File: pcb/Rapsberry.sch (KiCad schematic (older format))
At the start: 1 part, among them P1 CONN_RASPBERRY

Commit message: getting  roo for sensors
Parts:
- P1: footprint TH:RPI_MATRIX_40 -> SMD:SMD_CONN_2x20
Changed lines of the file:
@@
 $Descr A4 11693 8268
 encoding utf-8
-Sheet 7 8
+Sheet 6 8
 Title ""
 Date ""
@@
 F 0 "P1" H 3825 3565 50  0000 C CNN
 F 1 "CONN_RASPBERRY" H 3825 3474 50  0000 C CNN
-F 2 "TH:RPI_MATRIX_40" H 3825 3481 60  0001 C CNN
+F 2 "SMD:SMD_CONN_2x20" H 3825 3481 60  0001 C CNN
 F 3 "" H 3300 1450 60  0000 C CNN
 	1    4100 2400

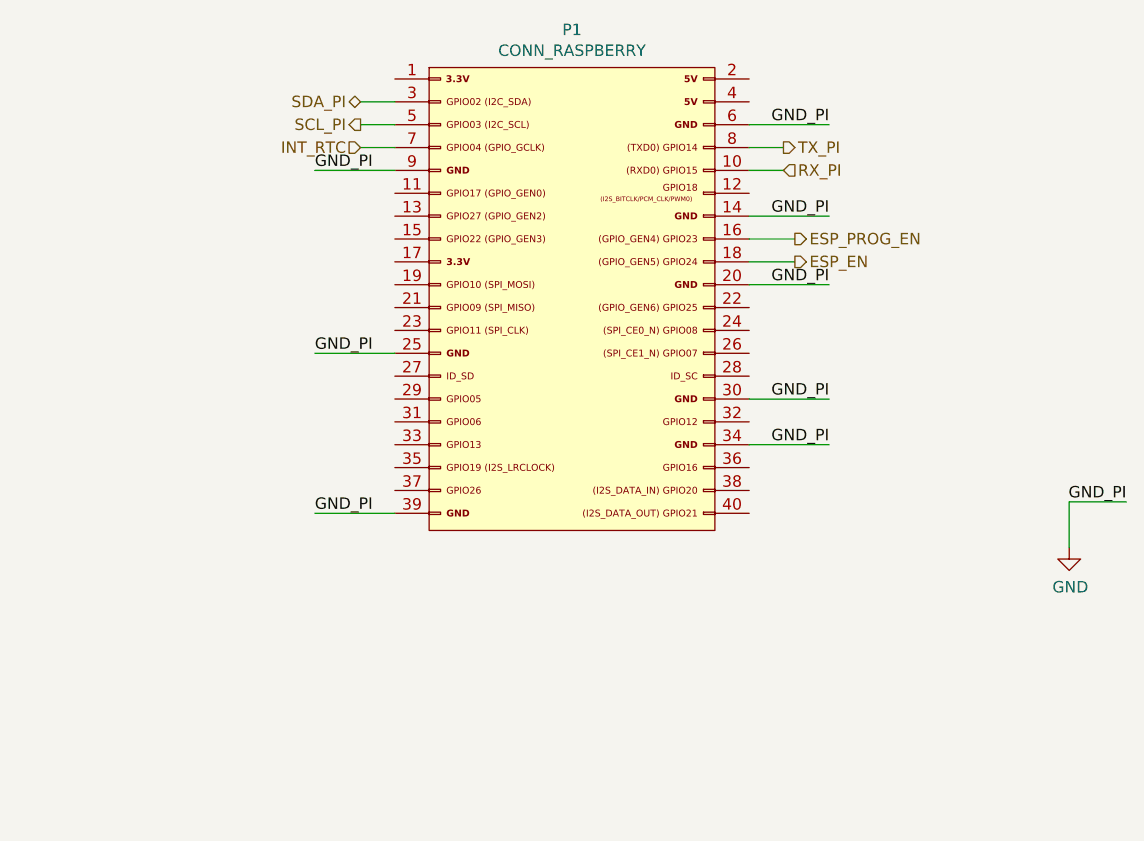
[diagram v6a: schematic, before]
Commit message: SPI connections between FPGA, PI and FLASH
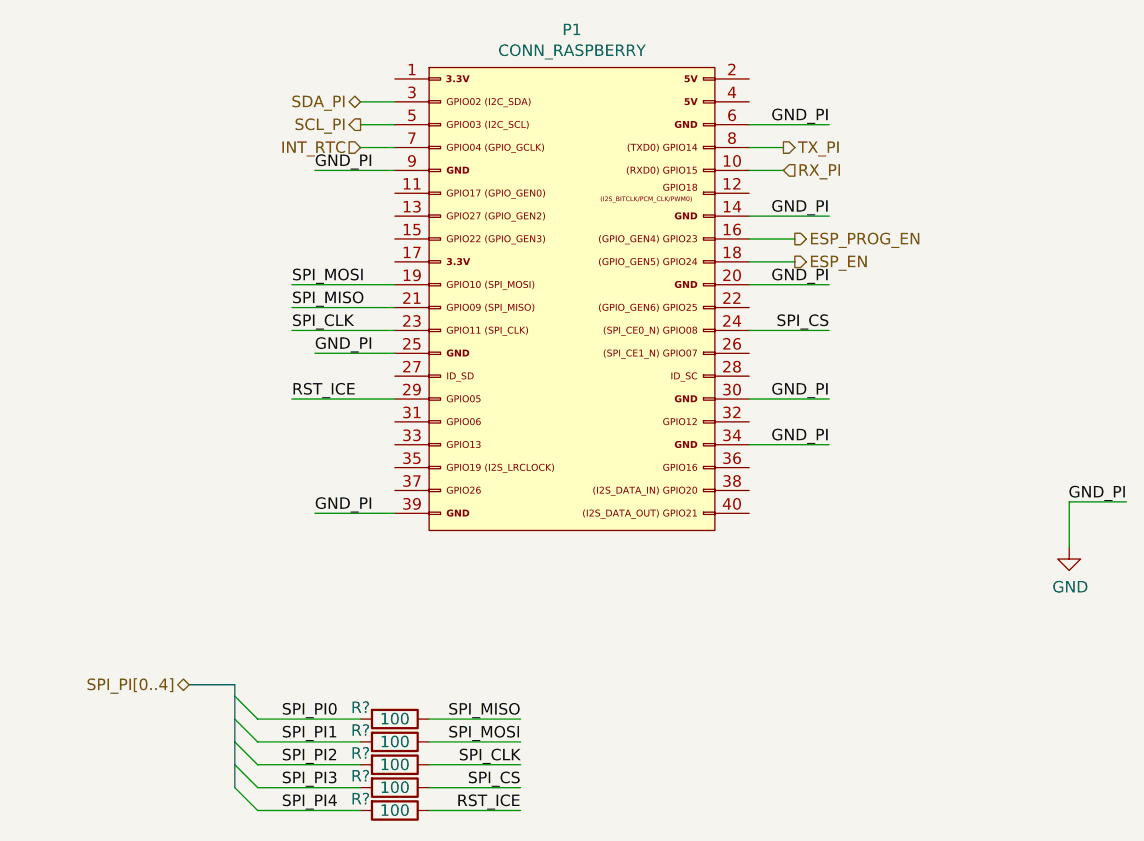
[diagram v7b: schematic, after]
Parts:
- added R? (x5): 100, symbol Device:R
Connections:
- net SPI_MOSI: now reaches P1.19 (P19)
- net SPI_MOSI: now also R?.1
- net SPI_MISO: now reaches P1.21 (P21)
- net SPI_MISO: now also R?.1
- net SPI_CLK: now reaches P1.23 (P23)
- net SPI_CLK: now also R?.1
- net SPI_CS: now reaches P1.24 (P24)
- net SPI_CS: now also R?.1
- net RST_ICE: now reaches P1.29 (P29)
- net RST_ICE: now also R?.1
- new net SPI_PI0: R?.2
- new net SPI_PI1: R?.2
- new net SPI_PI2: R?.2
- new net SPI_PI3: R?.2
- new net SPI_PI4: R?.2
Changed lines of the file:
@@
 Text Label 6250 3300 2    50   ~ 0
 GND_PI
+Text HLabel 2150 4100 0    50   BiDi ~ 0
+SPI_PI[0..4]
+Wire Bus Line
+	2150 4100 2350 4100
+Entry Wire Line
+	2350 4150 2450 4250
+Entry Wire Line
+	2350 4250 2450 4350
+Entry Wire Line
+	2350 4350 2450 4450
+Entry Wire Line
+	2350 4450 2450 4550
+Entry Wire Line
+	2350 4550 2450 4650
+Text Label 2800 4250 2    50   ~ 0
+SPI_PI0
+Text Label 2800 4350 2    50   ~ 0
+SPI_PI1
+Text Label 2800 4450 2    50   ~ 0
+SPI_PI2
+Text Label 2800 4550 2    50   ~ 0
+SPI_PI3
+Text Label 2800 4650 2    50   ~ 0
+SPI_PI4
+Text Label 2600 2350 0    50   ~ 0
+SPI_MOSI
+Text Label 2600 2450 0    50   ~ 0
+SPI_MISO
+Text Label 2600 2550 0    50   ~ 0
+SPI_CLK
+Text Label 4950 2550 2    50   ~ 0
+SPI_CS
+Wire Wire Line
+	2600 2350 3050 2350
+Wire Wire Line
+	2600 2450 3050 2450
+Wire Wire Line
+	2600 2550 3050 2550
+Wire Wire Line
+	4950 2550 4600 2550
+Text Label 3600 4250 2    50   ~ 0
+SPI_MISO
+Text Label 3600 4350 2    50   ~ 0
+SPI_MOSI
+Text Label 3600 4450 2    50   ~ 0
+SPI_CLK
+Text Label 3600 4550 2    50   ~ 0
+SPI_CS
+Text Label 2600 2850 0    50   ~ 0
+RST_ICE
+Wire Wire Line
+	2600 2850 3050 2850
+Text Label 3600 4650 2    50   ~ 0
+RST_ICE
+Wire Wire Line
+	2450 4250 2900 4250
+Wire Wire Line
+	2450 4350 2900 4350
+Wire Wire Line
+	2450 4450 2900 4450
+Wire Wire Line
+	2450 4550 2900 4550
+Wire Wire Line
+	2450 4650 2900 4650
+$Comp
+L Device:R R?
+U 1 1 5E9EA326
+P 3050 4250
+F 0 "R?" V 3000 4100 50  0000 C CNN
+F 1 "100" V 3050 4250 50  0000 C CNN
+F 2 "" V 2980 4250 50  0001 C CNN
+F 3 "~" H 3050 4250 50  0001 C CNN
+	1    3050 4250
+	0    1    1    0
+$EndComp
+$Comp
+L Device:R R?
+U 1 1 5EA15CD3
+P 3050 4350
+F 0 "R?" V 3000 4200 50  0000 C CNN
+F 1 "100" V 3050 4350 50  0000 C CNN
+F 2 "" V 2980 4350 50  0001 C CNN
+F 3 "~" H 3050 4350 50  0001 C CNN
+	1    3050 4350
+	0    1    1    0
+$EndComp
+$Comp
+L Device:R R?
+U 1 1 5EA17179
+P 3050 4450
+F 0 "R?" V 3000 4300 50  0000 C CNN
+F 1 "100" V 3050 4450 50  0000 C CNN
+F 2 "" V 2980 4450 50  0001 C CNN
+F 3 "~" H 3050 4450 50  0001 C CNN
+	1    3050 4450
+	0    1    1    0
+$EndComp
+$Comp
+L Device:R R?
+U 1 1 5EA17183
+P 3050 4550
+F 0 "R?" V 3000 4400 50  0000 C CNN
+F 1 "100" V 3050 4550 50  0000 C CNN
+F 2 "" V 2980 4550 50  0001 C CNN
+F 3 "~" H 3050 4550 50  0001 C CNN
+	1    3050 4550
+	0    1    1    0
+$EndComp
+$Comp
+L Device:R R?
+U 1 1 5EA17F2D
+P 3050 4650
+F 0 "R?" V 3000 4500 50  0000 C CNN
+F 1 "100" V 3050 4650 50  0000 C CNN
+F 2 "" V 2980 4650 50  0001 C CNN
+F 3 "~" H 3050 4650 50  0001 C CNN
+	1    3050 4650
+	0    1    1    0
+$EndComp
+Wire Wire Line
+	3600 4250 3200 4250
+Wire Wire Line
+	3600 4350 3200 4350
+Wire Wire Line
+	3600 4450 3200 4450
+Wire Wire Line
+	3600 4550 3200 4550
+Wire Wire Line
+	3600 4650 3200 4650
+Wire Bus Line
+	2350 4100 2350 4550
 $EndSCHEMATC

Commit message: stm32 jtag  connected
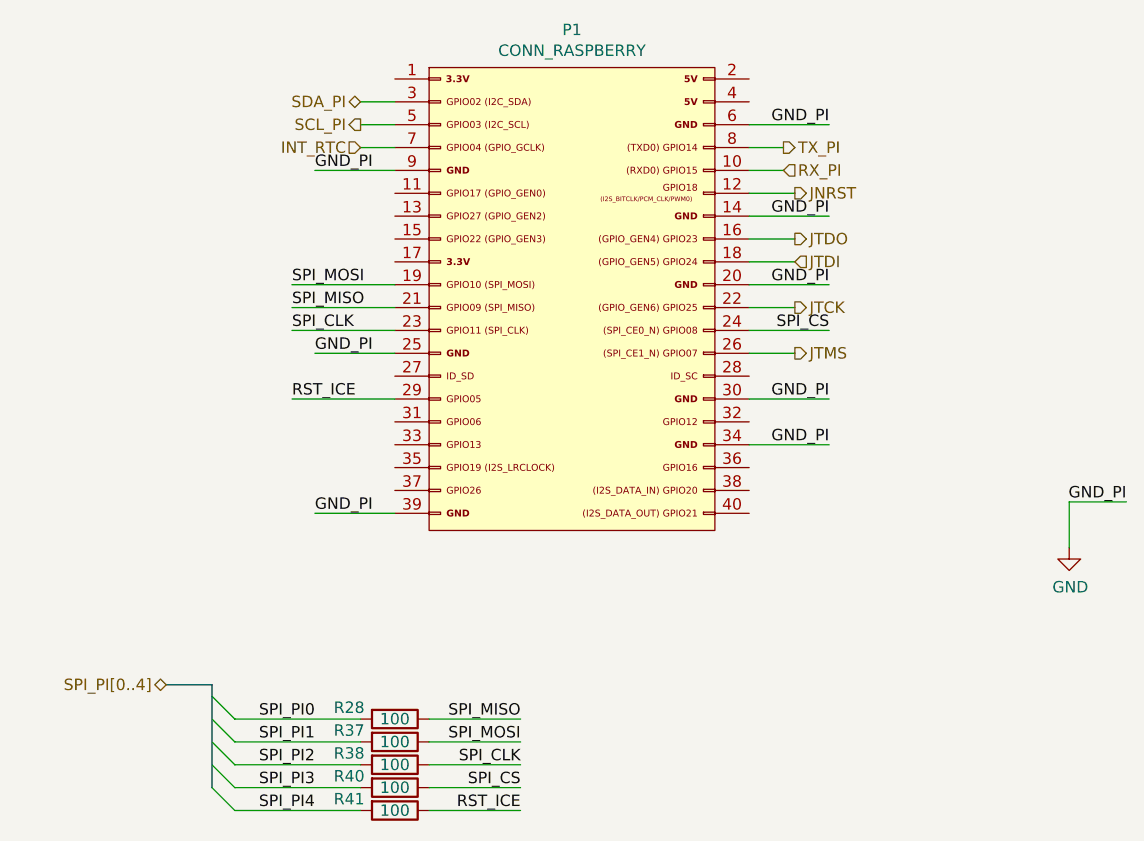
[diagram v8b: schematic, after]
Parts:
- R28, R37, R38, R40, R41: renamed from R?; footprint (none) -> Resistor_SMD:R_0402_1005Metric
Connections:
- net JNRST: now reaches P1.12 (P12)
- net JTCK: now reaches P1.22 (P22)
- net JTMS: now reaches P1.26 (P26)
- net ESP_EN renamed JTDI
- net ESP_PROG_EN renamed JTDO
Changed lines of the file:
@@
 EESchema Schematic File Version 4
+LIBS:keep_breathing_ctrl-cache
 EELAYER 30 0
 EELAYER END
 $Descr A4 11693 8268
 encoding utf-8
-Sheet 5 9
+Sheet 9 9
 Title ""
 Date ""
@@
 Wire Wire Line
 	4600 1850 4750 1850
-Text HLabel 4800 2150 2    50   Output ~ 0
-ESP_PROG_EN
-Text HLabel 4800 2250 2    50   Output ~ 0
-ESP_EN
 Wire Wire Line
 	4600 2150 4800 2150
@@
 Text Label 6250 3300 2    50   ~ 0
 GND_PI
-Text HLabel 2150 4100 0    50   BiDi ~ 0
+Text HLabel 2050 4100 0    50   BiDi ~ 0
 SPI_PI[0..4]
 Wire Bus Line
-	2150 4100 2350 4100
-Entry Wire Line
-	2350 4150 2450 4250
-Entry Wire Line
-	2350 4250 2450 4350
-Entry Wire Line
-	2350 4350 2450 4450
-Entry Wire Line
-	2350 4450 2450 4550
-Entry Wire Line
-	2350 4550 2450 4650
-Text Label 2800 4250 2    50   ~ 0
+	2050 4100 2250 4100
+Entry Wire Line
+	2250 4150 2350 4250
+Entry Wire Line
+	2250 4250 2350 4350
+Entry Wire Line
+	2250 4350 2350 4450
+Entry Wire Line
+	2250 4450 2350 4550
+Entry Wire Line
+	2250 4550 2350 4650
+Text Label 2700 4250 2    50   ~ 0
 SPI_PI0
-Text Label 2800 4350 2    50   ~ 0
+Text Label 2700 4350 2    50   ~ 0
 SPI_PI1
-Text Label 2800 4450 2    50   ~ 0
+Text Label 2700 4450 2    50   ~ 0
 SPI_PI2
-Text Label 2800 4550 2    50   ~ 0
+Text Label 2700 4550 2    50   ~ 0
 SPI_PI3
-Text Label 2800 4650 2    50   ~ 0
+Text Label 2700 4650 2    50   ~ 0
 SPI_PI4
 Text Label 2600 2350 0    50   ~ 0
@@
 RST_ICE
 Wire Wire Line
-	2450 4250 2900 4250
-Wire Wire Line
-	2450 4350 2900 4350
-Wire Wire Line
-	2450 4450 2900 4450
-Wire Wire Line
-	2450 4550 2900 4550
-Wire Wire Line
-	2450 4650 2900 4650
-$Comp
-L Device:R R?
+	2350 4250 2900 4250
+Wire Wire Line
+	2350 4350 2900 4350
+Wire Wire Line
+	2350 4450 2900 4450
+Wire Wire Line
+	2350 4550 2900 4550
+Wire Wire Line
+	2350 4650 2900 4650
+$Comp
+L Device:R R28
 U 1 1 5E9EA326
 P 3050 4250
-F 0 "R?" V 3000 4100 50  0000 C CNN
+F 0 "R28" V 3000 4050 50  0000 C CNN
 F 1 "100" V 3050 4250 50  0000 C CNN
-F 2 "" V 2980 4250 50  0001 C CNN
+F 2 "Resistor_SMD:R_0402_1005Metric" V 2980 4250 50  0001 C CNN
 F 3 "~" H 3050 4250 50  0001 C CNN
 	1    3050 4250
@@
 $EndComp
 $Comp
-L Device:R R?
+L Device:R R37
 U 1 1 5EA15CD3
 P 3050 4350
-F 0 "R?" V 3000 4200 50  0000 C CNN
+F 0 "R37" V 3000 4150 50  0000 C CNN
 F 1 "100" V 3050 4350 50  0000 C CNN
-F 2 "" V 2980 4350 50  0001 C CNN
+F 2 "Resistor_SMD:R_0402_1005Metric" V 2980 4350 50  0001 C CNN
 F 3 "~" H 3050 4350 50  0001 C CNN
 	1    3050 4350
@@
 $EndComp
 $Comp
-L Device:R R?
+L Device:R R38
 U 1 1 5EA17179
 P 3050 4450
-F 0 "R?" V 3000 4300 50  0000 C CNN
+F 0 "R38" V 3000 4250 50  0000 C CNN
 F 1 "100" V 3050 4450 50  0000 C CNN
-F 2 "" V 2980 4450 50  0001 C CNN
+F 2 "Resistor_SMD:R_0402_1005Metric" V 2980 4450 50  0001 C CNN
 F 3 "~" H 3050 4450 50  0001 C CNN
 	1    3050 4450
@@
 $EndComp
 $Comp
-L Device:R R?
+L Device:R R40
 U 1 1 5EA17183
 P 3050 4550
-F 0 "R?" V 3000 4400 50  0000 C CNN
+F 0 "R40" V 3000 4350 50  0000 C CNN
 F 1 "100" V 3050 4550 50  0000 C CNN
-F 2 "" V 2980 4550 50  0001 C CNN
+F 2 "Resistor_SMD:R_0402_1005Metric" V 2980 4550 50  0001 C CNN
 F 3 "~" H 3050 4550 50  0001 C CNN
 	1    3050 4550
@@
 $EndComp
 $Comp
-L Device:R R?
+L Device:R R41
 U 1 1 5EA17F2D
 P 3050 4650
-F 0 "R?" V 3000 4500 50  0000 C CNN
+F 0 "R41" V 3000 4450 50  0000 C CNN
 F 1 "100" V 3050 4650 50  0000 C CNN
-F 2 "" V 2980 4650 50  0001 C CNN
+F 2 "Resistor_SMD:R_0402_1005Metric" V 2980 4650 50  0001 C CNN
 F 3 "~" H 3050 4650 50  0001 C CNN
 	1    3050 4650
@@
 Wire Wire Line
 	3600 4650 3200 4650
+Text HLabel 4800 2650 2    50   Output ~ 0
+JTMS
+Text HLabel 4800 2450 2    50   Output ~ 0
+JTCK
+Text HLabel 4800 2250 2    50   Input ~ 0
+JTDI
+Text HLabel 4800 2150 2    50   Output ~ 0
+JTDO
+Wire Wire Line
+	4800 2450 4600 2450
+Wire Wire Line
+	4800 2650 4600 2650
+Wire Wire Line
+	4800 1950 4600 1950
+Text HLabel 4800 1950 2    50   Output ~ 0
+JNRST
 Wire Bus Line
-	2350 4100 2350 4550
+	2250 4100 2250 4550
 $EndSCHEMATC
